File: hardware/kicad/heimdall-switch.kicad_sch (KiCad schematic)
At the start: 42 parts, among them J1 SWD (ARM 10-pin), J2 LOAD_OUT, J3 BATT_IN, J4 B3B-XH-A, Q1 AO3400A, Q2 BSS84, Q3 AO4407A, Q4 AO4407A, Q5 AO3400A, Q6 BSS84, SW1 PTS810, U1 BT832, U2 TPS629206, Y1 32.768kHz

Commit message: Main PCB: narrow wire tabs per pair, +/- pads 3.5mm apart
Each wire pair sits on its own 7.3mm tab (straight edges, 1mm corner
radii, 4mm past the pads), SPS-20 style. New project footprint
SolderWire-0.75sqmm_1x02_P3.5mm (KiCad's P4.8mm with pad 2 moved).
No GND pour on the tab extensions or around the + pads on B (rule
areas). +/- marked on silk. Re-routed with the usual pipeline: 42 vias,
~590mm. ERC/DRC clean, full parity.

Co-Authored-By: Claude Opus 5.5 <noreply@anthropic.com>
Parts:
- J2, J3: footprint Connector_Wire:SolderWire-0.75sqmm_1x02_P4.8mm_D1.25mm_OD2.3mm -> heimdall-switch:SolderWire-0.75sqmm_1x02_P3.5mm_D1.25mm_OD2.3mm
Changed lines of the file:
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@@
 			)
 		)
-		(property "Footprint" "Connector_Wire:SolderWire-0.75sqmm_1x02_P4.8mm_D1.25mm_OD2.3mm"
+		(property "Footprint" "heimdall-switch:SolderWire-0.75sqmm_1x02_P3.5mm_D1.25mm_OD2.3mm"
 			(at 69.85 102.87 0)
 			(hide yes)
@@
 			)
 		)
-		(property "Footprint" "Connector_Wire:SolderWire-0.75sqmm_1x02_P4.8mm_D1.25mm_OD2.3mm"
+		(property "Footprint" "heimdall-switch:SolderWire-0.75sqmm_1x02_P3.5mm_D1.25mm_OD2.3mm"
 			(at 160.02 180.34 0)
 			(hide yes)

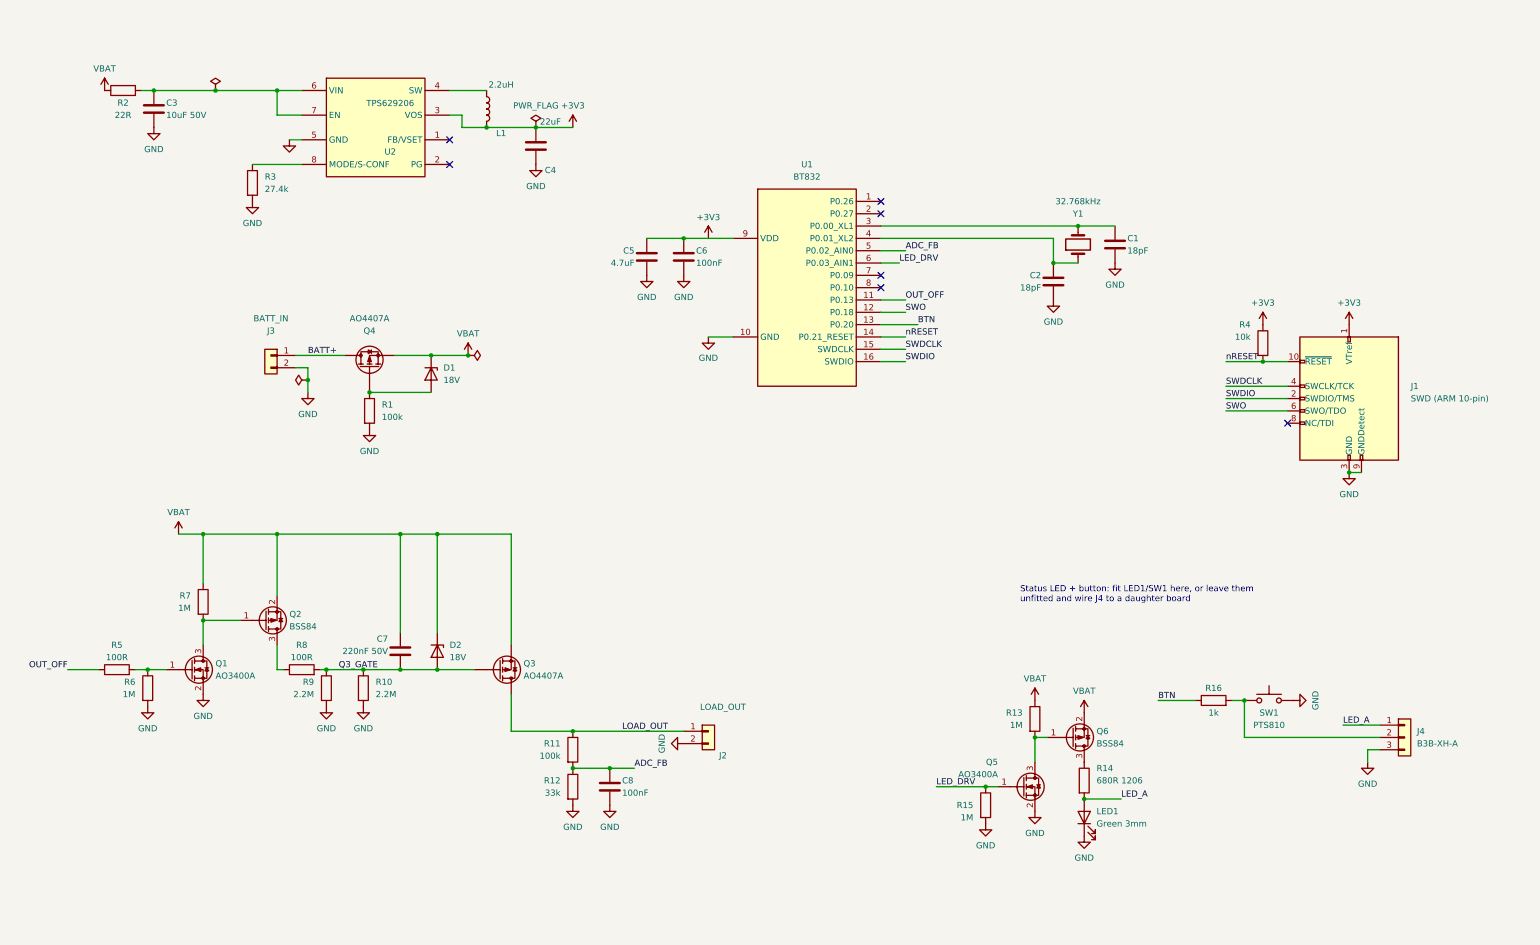
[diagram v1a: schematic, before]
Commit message: Schematic + docs: block-by-block notes on how the circuit works
Text note per functional block on the sheet (battery/reverse polarity,
fail-on load switch and its off chain, load sense, regulator, MCU,
LED/button), and a matching 'circuit at a glance' table at the top of
the Schematic section in hardware.md. ERC clean.

Co-Authored-By: Claude Opus 5.5 <noreply@anthropic.com>
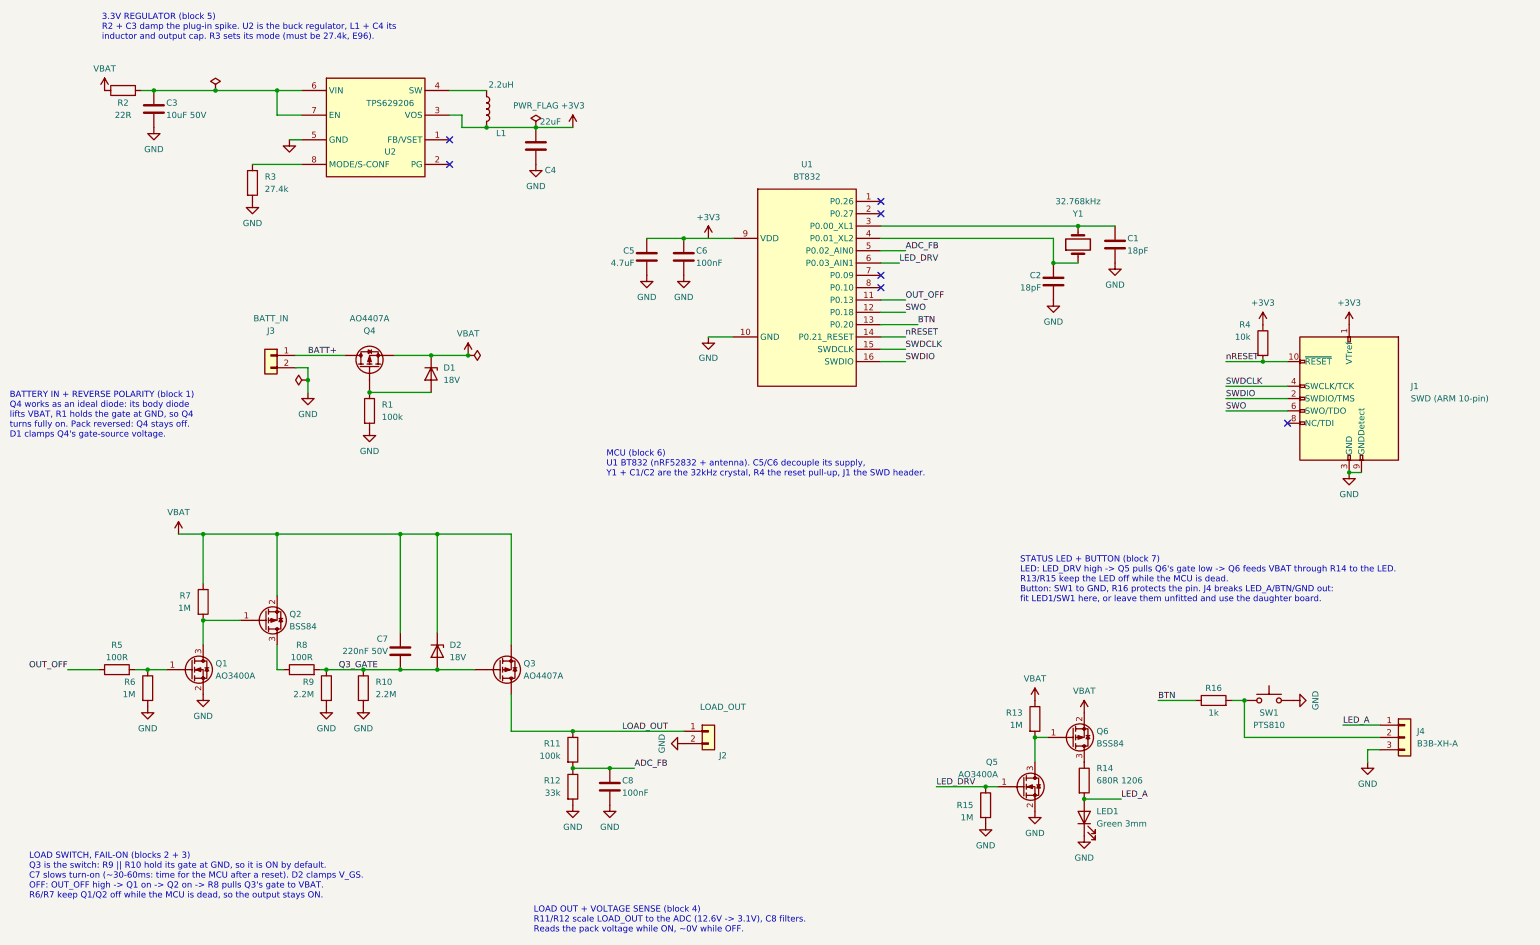
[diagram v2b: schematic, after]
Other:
- note added: "3.3V REGULATOR (block 5) R2 + C3 damp the plug-in spike. U2 is the buck regulator, L1 + C4 its inductor and output cap. R3 sets its mode (must be 27.4k, E96)."
- note added: "BATTERY IN + REVERSE POLARITY (block 1) Q4 works as an ideal diode: its body diode lifts VBAT, R1 holds the gate at GND, so Q4 turns fully on. Pack reversed: Q4 stays off. D1 clamps Q4's gate-source voltage."
- note added: "LOAD OUT + VOLTAGE SENSE (block 4) R11/R12 scale LOAD_OUT to the ADC (12.6V -> 3.1V), C8 filters. Reads the pack voltage while ON, ~0V while OFF."
- note added: "LOAD SWITCH, FAIL-ON (blocks 2 + 3) Q3 is the switch: R9 || R10 hold its gate at GND, so it is ON by default. C7 slows turn-on (~30-60ms: time for the MCU after a reset). D2 clamps V_GS. OFF: OUT_OFF high -> Q1 on -> Q2 on -> R8 pulls Q3's gate to VBAT. R6/R7 keep Q1/Q2 off while the MCU is dead, so the output stays ON."
- note added: "MCU (block 6) U1 BT832 (nRF52832 + antenna). C5/C6 decouple its supply, Y1 + C1/C2 are the 32kHz crystal, R4 the reset pull-up, J1 the SWD header."
- note added: "STATUS LED + BUTTON (block 7) LED: LED_DRV high -> Q5 pulls Q6's gate low -> Q6 feeds VBAT through R14 to the LED. R13/R15 keep the LED off while the MCU is dead. Button: SW1 to GND, R16 protects the pin. J4 breaks LED_A/BTN/GND out: fit LED1/SW1 here, or leave them unfitted and use the daughter board."
- note removed: "Status LED + button: fit LED1/SW1 here, or leave them unfitted and wire J4 to a daughter board"
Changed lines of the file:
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@@
 	(generator_version "10.0")
 	(paper "A3")
-	(text "Status LED + button: fit LED1/SW1 here, or leave them\nunfitted and wire J4 to a daughter board"
+	(text "3.3V REGULATOR (block 5)\nR2 + C3 damp the plug-in spike. U2 is the buck regulator, L1 + C4 its\ninductor and output cap. R3 sets its mode (must be 27.4k, E96)."
+		(exclude_from_sim no)
+		(at 35 38 0)
+		(effects
+			(font
+				(size 1.27 1.27)
+			)
+			(justify left bottom)
+		)
+	)
+	(text "BATTERY IN + REVERSE POLARITY (block 1)\nQ4 works as an ideal diode: its body diode\nlifts VBAT, R1 holds the gate at GND, so Q4\nturns fully on. Pack reversed: Q4 stays off.\nD1 clamps Q4's gate-source voltage."
+		(exclude_from_sim no)
+		(at 16 120 0)
+		(effects
+			(font
+				(size 1.27 1.27)
+			)
+			(justify left bottom)
+		)
+	)
+	(text "LOAD SWITCH, FAIL-ON (blocks 2 + 3)\nQ3 is the switch: R9 || R10 hold its gate at GND, so it is ON by default.\nC7 slows turn-on (~30-60ms: time for the MCU after a reset). D2 clamps V_GS.\nOFF: OUT_OFF high -> Q1 on -> Q2 on -> R8 pulls Q3's gate to VBAT.\nR6/R7 keep Q1/Q2 off while the MCU is dead, so the output stays ON."
+		(exclude_from_sim no)
+		(at 20 215 0)
+		(effects
+			(font
+				(size 1.27 1.27)
+			)
+			(justify left bottom)
+		)
+	)
+	(text "LOAD OUT + VOLTAGE SENSE (block 4)\nR11/R12 scale LOAD_OUT to the ADC (12.6V -> 3.1V), C8 filters.\nReads the pack voltage while ON, ~0V while OFF."
+		(exclude_from_sim no)
+		(at 124 222 0)
+		(effects
+			(font
+				(size 1.27 1.27)
+			)
+			(justify left bottom)
+		)
+	)
+	(text "MCU (block 6)\nU1 BT832 (nRF52832 + antenna). C5/C6 decouple its supply,\nY1 + C1/C2 are the 32kHz crystal, R4 the reset pull-up, J1 the SWD header."
+		(exclude_from_sim no)
+		(at 139 128 0)
+		(effects
+			(font
+				(size 1.27 1.27)
+			)
+			(justify left bottom)
+		)
+	)
+	(text "STATUS LED + BUTTON (block 7)\nLED: LED_DRV high -> Q5 pulls Q6's gate low -> Q6 feeds VBAT through R14 to the LED.\nR13/R15 keep the LED off while the MCU is dead.\nButton: SW1 to GND, R16 protects the pin. J4 breaks LED_A/BTN/GND out:\nfit LED1/SW1 here, or leave them unfitted and use the daughter board."
 		(exclude_from_sim no)
 		(at 224.282 153.924 0)

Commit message: Main PCB: J4 JST-XH -> JST-GH right-angle SMD (SM03B-GHS-TB)
J4 now sits at the right edge with its cable entry flush with the board
edge. LED_A runs on F.Cu to LED1, J4 pin 2 reaches R16 through one via
under the connector body, and /BTN on B.Cu no longer detours around the
old XH holes. Rev 1 of the main board (not ordered).

Co-Authored-By: Claude Opus 5.5 <noreply@anthropic.com>
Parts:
- J4: value B3B-XH-A -> SM03B-GHS-TB; footprint Connector_JST:JST_XH_B3B-XH-A_1x03_P2.50mm_Vertical -> Connector_JST:JST_GH_SM03B-GHS-TB_1x03-1MP_P1.25mm_Horizontal; LCSC C144394 -> C514175
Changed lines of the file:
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@@
 			)
 		)
-		(property "Value" "B3B-XH-A"
+		(property "Value" "SM03B-GHS-TB"
 			(at 306.07 182.88 0)
 			(show_name no)
@@
 			)
 		)
-		(property "Footprint" "Connector_JST:JST_XH_B3B-XH-A_1x03_P2.50mm_Vertical"
+		(property "Footprint" "Connector_JST:JST_GH_SM03B-GHS-TB_1x03-1MP_P1.25mm_Horizontal"
 			(at 303.53 181.61 0)
 			(hide yes)
@@
 			)
 		)
-		(property "LCSC" "C144394"
+		(property "LCSC" "C514175"
 			(at 303.53 181.61 0)
 			(hide yes)

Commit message: Source the prototype run from TME and Mouser
Add hidden Manufacturer/MPN/Supplier/Supplier PN fields to both
schematics for the parts actually ordered; the LCSC fields stay as the
alternative source, so jlc_export.py is unchanged. Mouser takes the
BT832, TPS629206, L1 and Y1, TME the rest.

Substitutes where the original is out of stock or not carried at TME
and Mouser (checked against datasheets and the design notes): Yageo RC
resistors, BSS84AK, CL31A106 (X5R) for C3, Murata 22uF for C4,
DC Components MMSZ5248B, Kingbright L-7104ZGCK LED and Connfly
DS1031-08 SWD header (land pattern within ~0.1mm of the stock
footprint).

order_export.py writes the TME basket import and Mouser BOM files
from the schematic fields; hardware.md's BOM and cost estimate are
updated to the 2026-10-04 prices.

Co-Authored-By: Claude Opus 5.5 <noreply@anthropic.com>
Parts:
- C1, C2: MPN (none) -> CL10C180JB8NNNC; Manufacturer (none) -> Samsung; Supplier (none) -> TME; Supplier PN (none) -> CL10C180JB8NNNC
- C3: MPN (none) -> CL31A106KBHNNNE; Manufacturer (none) -> Samsung; Supplier (none) -> TME; Supplier PN (none) -> CL31A106KBHNNNE
- C4: MPN (none) -> GRM21BR61E226ME44L; Manufacturer (none) -> Murata; Supplier (none) -> TME; Supplier PN (none) -> GRM21BR61E226ME44L
- C5: MPN (none) -> CL10A475KO8NNNC; Manufacturer (none) -> Samsung; Supplier (none) -> TME; Supplier PN (none) -> CL10A475KO8NNNC
- C6, C8: MPN (none) -> CC0603KRX7R9BB104; Manufacturer (none) -> Yageo; Supplier (none) -> TME; Supplier PN (none) -> CC0603KRX7R9BB104
- C7: MPN (none) -> CL21B224KBFNNNE; Manufacturer (none) -> Samsung; Supplier (none) -> TME; Supplier PN (none) -> CL21B224KBFNNNE
- D1, D2: MPN (none) -> MMSZ5248B; Manufacturer (none) -> DC Components; Supplier (none) -> TME; Supplier PN (none) -> MMSZ5248B-DC
- J1: MPN (none) -> DS1031-08-2*5P8BS41-3A; Manufacturer (none) -> Connfly; Supplier (none) -> TME; Supplier PN (none) -> ZL322-2X5P
- J4: MPN (none) -> SM03B-GHS-TB(LF)(SN); Manufacturer (none) -> JST; Supplier (none) -> TME; Supplier PN (none) -> SM03B-GHS-TB
- L1: MPN (none) -> DFE252012PD-2R2M=P2; Manufacturer (none) -> Murata; Supplier (none) -> Mouser; Supplier PN (none) -> 81-DFE252012PD2R2MP2
- LED1: MPN (none) -> L-7104ZGCK; Manufacturer (none) -> Kingbright; Supplier (none) -> TME; Supplier PN (none) -> L-7104ZGCK
- Q1, Q5: MPN (none) -> AO3400A; Manufacturer (none) -> Alpha & Omega; Supplier (none) -> TME; Supplier PN (none) -> AO3400A
- Q2, Q6: MPN (none) -> BSS84AK,215; Manufacturer (none) -> Nexperia; Supplier (none) -> TME; Supplier PN (none) -> BSS84AK.215
- Q3, Q4: MPN (none) -> AO4407A; Manufacturer (none) -> Alpha & Omega; Supplier (none) -> TME; Supplier PN (none) -> AO4407A
- R1, R11: MPN (none) -> RC0603FR-07100KL; Manufacturer (none) -> Yageo; Supplier (none) -> TME; Supplier PN (none) -> RC0603FR-07100K
- R10, R9: MPN (none) -> RC0603FR-072M2L; Manufacturer (none) -> Yageo; Supplier (none) -> TME; Supplier PN (none) -> RC0603FR-072M2
- R12: MPN (none) -> RC0603FR-0733KL; Manufacturer (none) -> Yageo; Supplier (none) -> TME; Supplier PN (none) -> RC0603FR-0733KL
- R13, R15, R6, R7: MPN (none) -> RC0603FR-071ML; Manufacturer (none) -> Yageo; Supplier (none) -> TME; Supplier PN (none) -> RC0603FR-071M
- R14: MPN (none) -> RC1206FR-07680RL; Manufacturer (none) -> Yageo; Supplier (none) -> TME; Supplier PN (none) -> RC1206FR-07680R
- R16: MPN (none) -> RC0603FR-071KL; Manufacturer (none) -> Yageo; Supplier (none) -> TME; Supplier PN (none) -> RC0603FR-071K
- R2: MPN (none) -> RC0603FR-0722RL; Manufacturer (none) -> Yageo; Supplier (none) -> TME; Supplier PN (none) -> RC0603FR-0722RL
- R3: MPN (none) -> RC0603FR-0727K4L; Manufacturer (none) -> Yageo; Supplier (none) -> TME; Supplier PN (none) -> RC0603FR-0727K4L
- R4: MPN (none) -> RC0603FR-0710KL; Manufacturer (none) -> Yageo; Supplier (none) -> TME; Supplier PN (none) -> RC0603FR-0710K
- R5, R8: MPN (none) -> RC0603FR-07100RL; Manufacturer (none) -> Yageo; Supplier (none) -> TME; Supplier PN (none) -> RC0603FR-07100R
- SW1: MPN (none) -> PTS810 SJM 250 SMTR LFS; Manufacturer (none) -> C&K; Supplier (none) -> TME; Supplier PN (none) -> PTS810SJM250SMTRLF
- U1: MPN (none) -> BT832; Manufacturer (none) -> Fanstel; Supplier (none) -> Mouser; Supplier PN (none) -> 308-BT832
- U2: MPN (none) -> TPS629206DRLR; Manufacturer (none) -> Texas Instruments; Supplier (none) -> Mouser; Supplier PN (none) -> 595-TPS629206DRLR
- Y1: MPN (none) -> FC-135 32.7680KA-A5; Manufacturer (none) -> Epson; Supplier (none) -> Mouser; Supplier PN (none) -> 732-532.7680KA-A5
